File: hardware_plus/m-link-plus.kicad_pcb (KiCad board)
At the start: 4 copper layers, 24 x 30 mm, 27 parts, among them J3 SIG, J4 PROGRAM, J5 I2C, SW1 RESTORE SETTINGS, U1 AP1117-33, U2 DRV8837C, U3 DRV8837C, U4 ESP-12F, U5 PCA9685PW, U6 DRV8837C

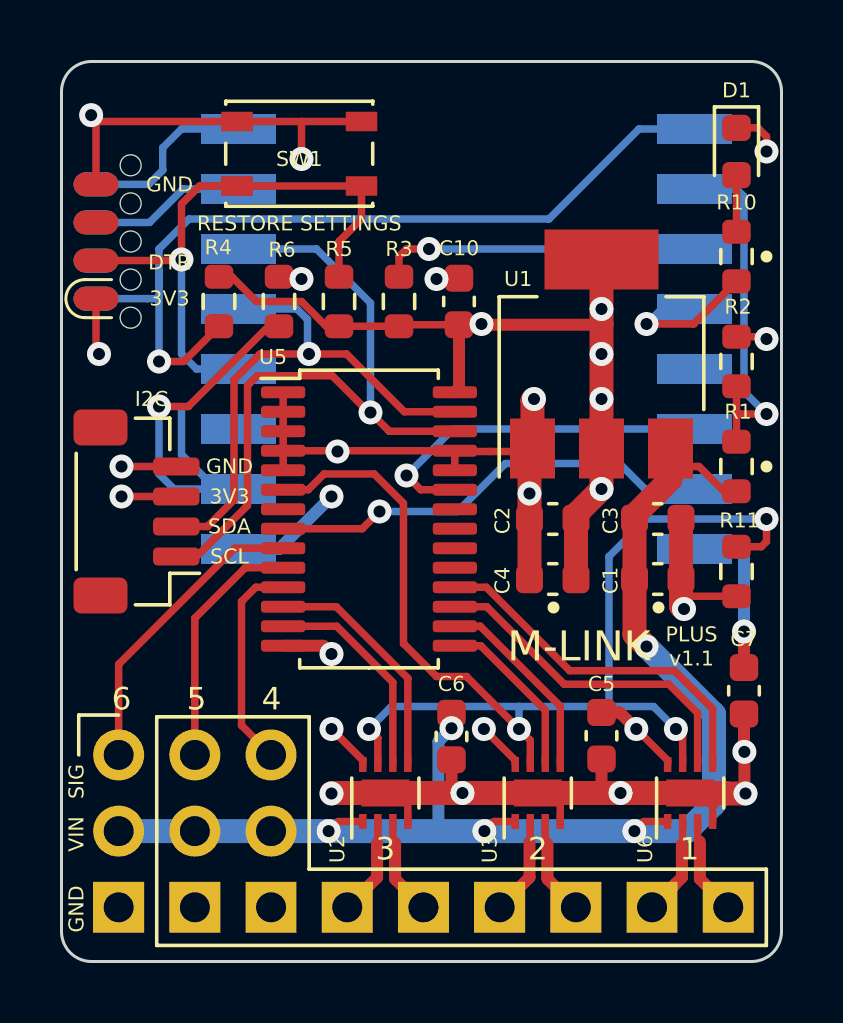
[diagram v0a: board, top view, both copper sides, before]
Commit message: Tidy up plus layout. Add plus HTML BOM.
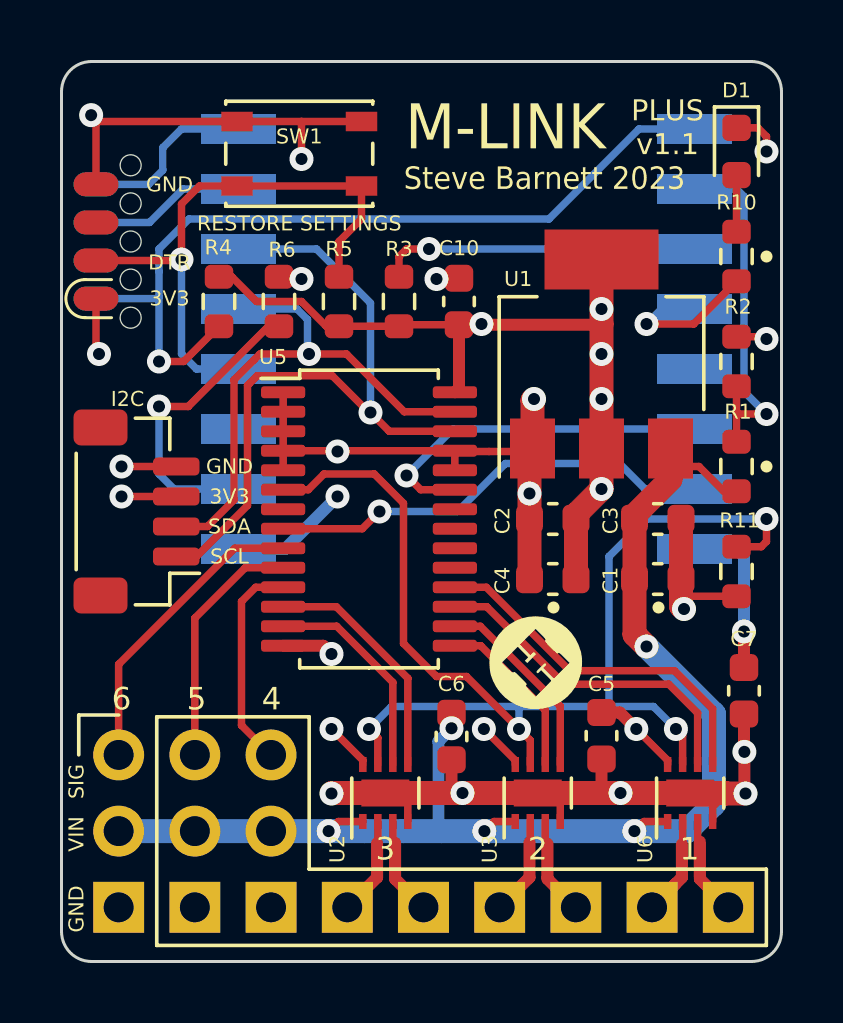
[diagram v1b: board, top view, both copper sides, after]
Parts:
- added G***: LOGO, new_moop_items:NottinghackLogo_4x4, F.Cu at (94.8, 89.0)
- added G***: LOGO, new_moop_items:NottinghackLogo_3x3, B.Cu at (84.8, 88.5)
- R1: value 33k -> 100k
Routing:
- net /MTDI: track 14.2 -> 10.2 mm
- net GND: track 86.7 -> 89.1 mm
- net /RESET: track 28.4 -> 27.9 mm
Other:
- board text added: "Steve Barnett 2023"
- board text removed: "Steve Barnett 2022"

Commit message: Version 1.1 ready for manufacture.
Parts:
- moved C7 0.45 mm to (101.5, 89.6)
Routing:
- net +3V3: track 42.9 -> 42.3 mm
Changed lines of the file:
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@@
   )
   (footprint "Capacitor_SMD:C_0603_1608Metric" (layer "F.Cu")
-    (at 101.75 89.975 -90)
+    (at 101.5 89.6 -90)
     (descr "Capacitor SMD 0603 (1608 Metric), square (rectangular) end terminal, IPC_7351 nominal, (Body size source: IPC-SM-782 page 76, https://www.pcb-3d.com/wordpress/wp-content/uploads/ipc-sm-782a_amendment_1_and_2.pdf), generated with kicad-footprint-generator")
     (tags "capacitor")
@@
     (style (thickness 0.15) (arrow_length 1.27) (text_position_mode 0) (extension_height 0.58642) (extension_offset 0.5) keep_text_aligned)
   )
-  (segment (start 101.762299 92.012299) (end 101.762299 93.362299) (width 0.4) (layer "F.Cu") (net 1))
   (segment (start 101.5 78.175) (end 102.425 78.175) (width 0.25) (layer "F.Cu") (net 1))
   (segment (start 95.716 93.384) (end 96.884 93.384) (width 0.8) (layer "F.Cu") (net 1))
@@
   (segment (start 86.3875 80.025) (end 86.3875 82.625) (width 0.25) (layer "F.Cu") (net 1))
   (segment (start 101.5 86.825) (end 99.975 86.825) (width 0.25) (layer "F.Cu") (net 1))
+  (segment (start 101.762299 90.637299) (end 101.5 90.375) (width 0.4) (layer "F.Cu") (net 1))
   (segment (start 101.132 93.4) (end 101.8 93.4) (width 0.8) (layer "F.Cu") (net 1))
   (segment (start 94.875 93.384) (end 95.716 93.384) (width 0.8) (layer "F.Cu") (net 1))
@@
   (segment (start 92.1125 81.975) (end 86.3875 81.975) (width 0.25) (layer "F.Cu") (net 1))
   (segment (start 80.2 71) (end 79.987701 70.787701) (width 0.25) (layer "F.Cu") (net 1))
-  (segment (start 101.75 92) (end 101.762299 92.012299) (width 0.4) (layer "F.Cu") (net 1))
   (segment (start 89.795 93.384) (end 90.866 93.384) (width 0.8) (layer "F.Cu") (net 1))
   (segment (start 87 71) (end 84.85 71) (width 0.25) (layer "F.Cu") (net 1))
   (segment (start 94.6 82) (end 93.25 82) (width 0.25) (layer "F.Cu") (net 1))
-  (segment (start 101.75 90.75) (end 101.75 92) (width 0.4) (layer "F.Cu") (net 1))
   (segment (start 99.955 93.384) (end 101.116 93.384) (width 0.8) (layer "F.Cu") (net 1))
   (segment (start 97 92.25) (end 97 93.268) (width 0.4) (layer "F.Cu") (net 1))
@@
   (segment (start 92 93.268) (end 91.884 93.384) (width 0.4) (layer "F.Cu") (net 1))
   (segment (start 96.884 93.384) (end 99.955 93.384) (width 0.8) (layer "F.Cu") (net 1))
+  (segment (start 101.762299 93.362299) (end 101.8 93.4) (width 0.4) (layer "F.Cu") (net 1))
   (segment (start 100.705 94.334) (end 100.705 93.845) (width 0.25) (layer "F.Cu") (net 1))
   (segment (start 87.725 88.475) (end 88 88.75) (width 0.4) (layer "F.Cu") (net 1))
@@
   (segment (start 102.5 72) (end 102.5 71.5) (width 0.25) (layer "F.Cu") (net 1))
   (segment (start 99.65 84.25) (end 99.65 86.25) (width 0.8) (layer "F.Cu") (net 1))
-  (segment (start 101.762299 93.362299) (end 101.8 93.4) (width 0.4) (layer "F.Cu") (net 1))
+  (segment (start 101.762299 92.012299) (end 101.762299 90.637299) (width 0.4) (layer "F.Cu") (net 1))
   (segment (start 94.6 86.25) (end 94.6 84.25) (width 0.8) (layer "F.Cu") (net 1))
   (segment (start 90.545 94.334) (end 90.545 93.705) (width 0.25) (layer "F.Cu") (net 1))
@@
   (segment (start 99.65 86.25) (end 99.65 87.15) (width 0.8) (layer "F.Cu") (net 1))
   (segment (start 99.975 86.825) (end 99.65 87.15) (width 0.25) (layer "F.Cu") (net 1))
+  (segment (start 101.762299 92.012299) (end 101.762299 93.362299) (width 0.4) (layer "F.Cu") (net 1))
   (segment (start 101.116 93.384) (end 101.132 93.4) (width 0.8) (layer "F.Cu") (net 1))
   (segment (start 88.016 93.384) (end 88 93.4) (width 0.8) (layer "F.Cu") (net 1))
@@
   (segment (start 89.045 92.434) (end 89.045 92.295) (width 0.25) (layer "F.Cu") (net 18))
   (segment (start 92.25 77.775) (end 90.3 77.775) (width 0.25) (layer "F.Cu") (net 18))
+  (segment (start 101.5 88) (end 101.5 88.825) (width 0.4) (layer "F.Cu") (net 18))
   (segment (start 90.25 77.825) (end 88.25 77.825) (width 0.25) (layer "F.Cu") (net 18))
   (segment (start 97 75.6) (end 97 77.75) (width 0.8) (layer "F.Cu") (net 18))
@@
   (segment (start 99.205 92.295) (end 98.16 91.25) (width 0.25) (layer "F.Cu") (net 18))
   (segment (start 97 90.7) (end 97.61 90.7) (width 0.4) (layer "F.Cu") (net 18))
-  (segment (start 101.75 89.2) (end 101.75 88) (width 0.4) (layer "F.Cu") (net 18))
   (segment (start 96.975 77.775) (end 97 77.75) (width 0.4) (layer "F.Cu") (net 18))
   (segment (start 85.5 77) (end 87 77) (width 0.25) (layer "F.Cu") (net 18))
@@
   (via (at 98.16 91.25) (size 0.8) (drill 0.4) (layers "F.Cu" "B.Cu") (net 18))
   (via (at 80.25 78.75) (size 0.8) (drill 0.4) (layers "F.Cu" "B.Cu") (net 18))
-  (via (at 101.75 88) (size 0.8) (drill 0.4) (layers "F.Cu" "B.Cu") (net 18))
+  (via (at 101.5 88) (size 0.8) (drill 0.4) (layers "F.Cu" "B.Cu") (net 18))
   (via (at 81 83.5) (size 0.8) (drill 0.4) (layers "F.Cu" "B.Cu") (net 18))
   (via (at 97 83.25) (size 0.8) (drill 0.4) (layers "F.Cu" "B.Cu") (net 18))
   (via (at 93.08 91.25) (size 0.8) (drill 0.4) (layers "F.Cu" "B.Cu") (net 18))
   (via (at 93 77.75) (size 0.8) (drill 0.4) (layers "F.Cu" "B.Cu") (net 18))
-  (segment (start 101.75 85.5) (end 101.5 85.25) (width 0.4) (layer "B.Cu") (net 18))
-  (segment (start 101.75 88) (end 101.75 85.5) (width 0.4) (layer "B.Cu") (net 18))
-  (segment (start 101.5 85.25) (end 100.1 85.25) (width 0.4) (layer "B.Cu") (net 18))
+  (segment (start 101.5 85.6) (end 101.15 85.25) (width 0.4) (layer "B.Cu") (net 18))
+  (segment (start 101.15 85.25) (end 100.1 85.25) (width 0.4) (layer "B.Cu") (net 18))
+  (segment (start 101.5 88) (end 101.5 85.6) (width 0.4) (layer "B.Cu") (net 18))
   (segment (start 83.5 85.5) (end 85.2 83.8) (width 0.25) (layer "F.Cu") (net 19))
   (segment (start 89.925 81.325) (end 89.3 80.7) (width 0.25) (layer "F.Cu") (net 19))
@@
   (segment (start 90.045 94.334) (end 90.045 96.174) (width 0.25) (layer "F.Cu") (net 33))
   (segment (start 91.065 97.194) (end 90.12 96.249) (width 0.4) (layer "F.Cu") (net 33))
-  (segment (start 100.205 90.718604) (end 100.205 92.434) (width 0.25) (layer "F.Cu") (net 34))
   (segment (start 92.1125 87.175) (end 93.175 87.175) (width 0.25) (layer "F.Cu") (net 34))
   (segment (start 93.175 87.175) (end 95.756802 89.756802) (width 0.25) (layer "F.Cu") (net 34))
-  (segment (start 99.243198 89.756802) (end 100.205 90.718604) (width 0.25) (layer "F.Cu") (net 34))
-  (segment (start 95.756802 89.756802) (end 99.243198 89.756802) (width 0.25) (layer "F.Cu") (net 34))
-  (segment (start 99.429594 89.306802) (end 100.705 90.582208) (width 0.25) (layer "F.Cu") (net 35))
-  (segment (start 100.705 90.582208) (end 100.705 92.434) (width 0.25) (layer "F.Cu") (net 35))
+  (segment (start 95.756802 89.756802) (end 99.056802 89.756802) (width 0.25) (layer "F.Cu") (net 34))
+  (segment (start 100.205 92.434) (end 100.205 90.905) (width 0.25) (layer "F.Cu") (net 34))
+  (segment (start 100.205 90.905) (end 99.056802 89.756802) (width 0.25) (layer "F.Cu") (net 34))
   (segment (start 92.1125 86.525) (end 93.161396 86.525) (width 0.25) (layer "F.Cu") (net 35))
-  (segment (start 95.943198 89.306802) (end 99.429594 89.306802) (width 0.25) (layer "F.Cu") (net 35))
+  (segment (start 100.705 90.768604) (end 99.243198 89.306802) (width 0.25) (layer "F.Cu") (net 35))
+  (segment (start 99.243198 89.306802) (end 95.943198 89.306802) (width 0.25) (layer "F.Cu") (net 35))
   (segment (start 93.161396 86.525) (end 95.943198 89.306802) (width 0.25) (layer "F.Cu") (net 35))
+  (segment (start 100.705 92.434) (end 100.705 90.768604) (width 0.25) (layer "F.Cu") (net 35))
   (segment (start 98.685 97.194) (end 99.68 96.199) (width 0.4) (layer "F.Cu") (net 36))
   (segment (start 99.705 96.174) (end 98.685 97.194) (width 0.25) (layer "F.Cu") (net 36))
